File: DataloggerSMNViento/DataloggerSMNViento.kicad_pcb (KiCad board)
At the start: 2 copper layers, 85.7 x 137.2 mm, 26 parts, among them P1 CONN_02X20, P10 CONN_01X20, P11 CONN_01X20, P12 CONN_01X06, P13 CONN_01X06, P14 CONN_02X12, P15 CONN_02X12, P16 CONN_02X12, P17 CONN_02X12, P18 CONN_01X12, P19 CONN_01X12, P2 CONN_01X20, P20 CONN_01X12, P21 CONN_01X12, P3 CONN_02X20, P4 CONN_02X20, P5 CONN_01X19, P6 CONN_02X20, P7 CONN_01X20, P8 CONN_02X20, P9 CONN_02X20

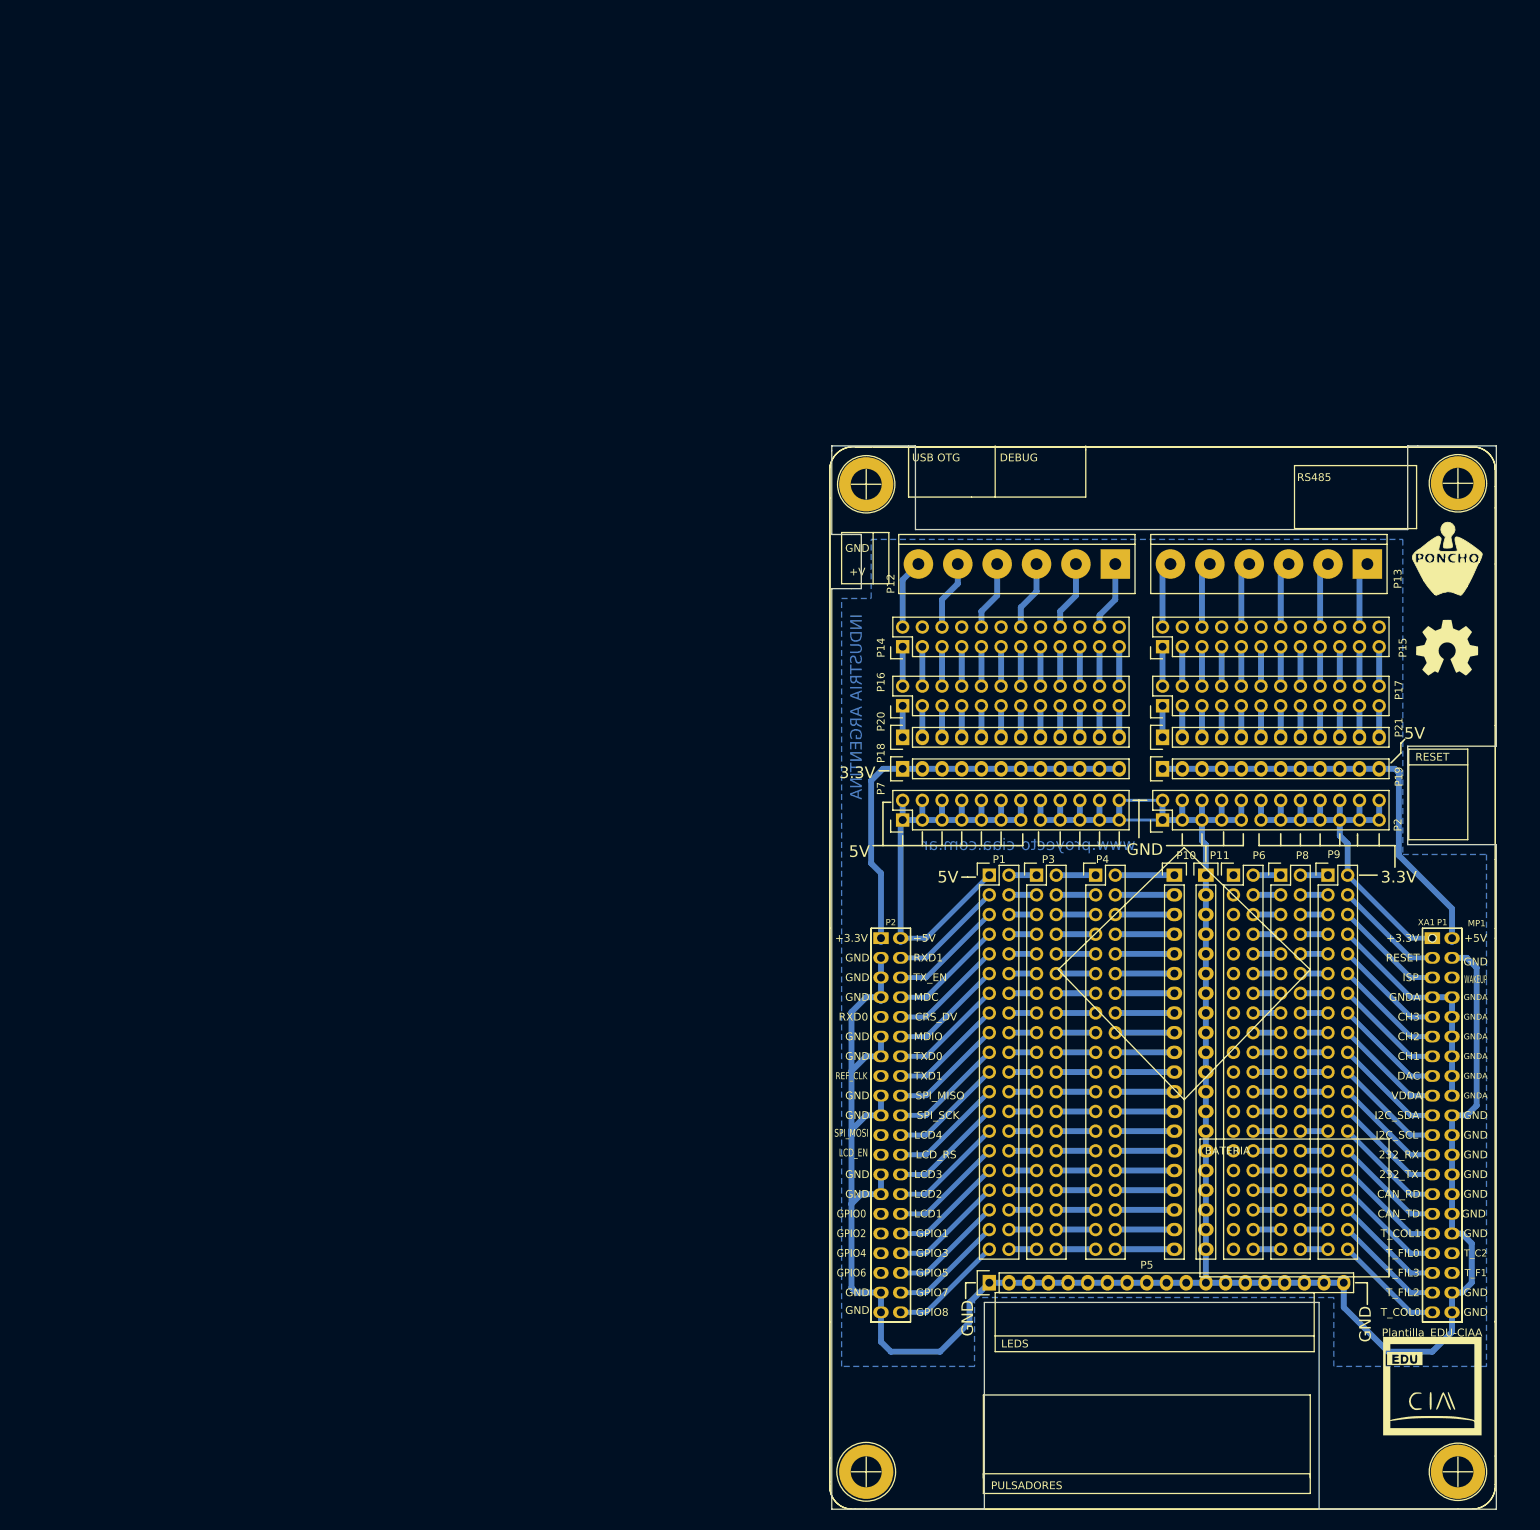
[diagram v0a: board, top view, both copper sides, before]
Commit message: Agrego modificaciones al poncho de la EDU CIAA, también agrego una simulacion del circuito para tomar la tensión del ADC del tunnel
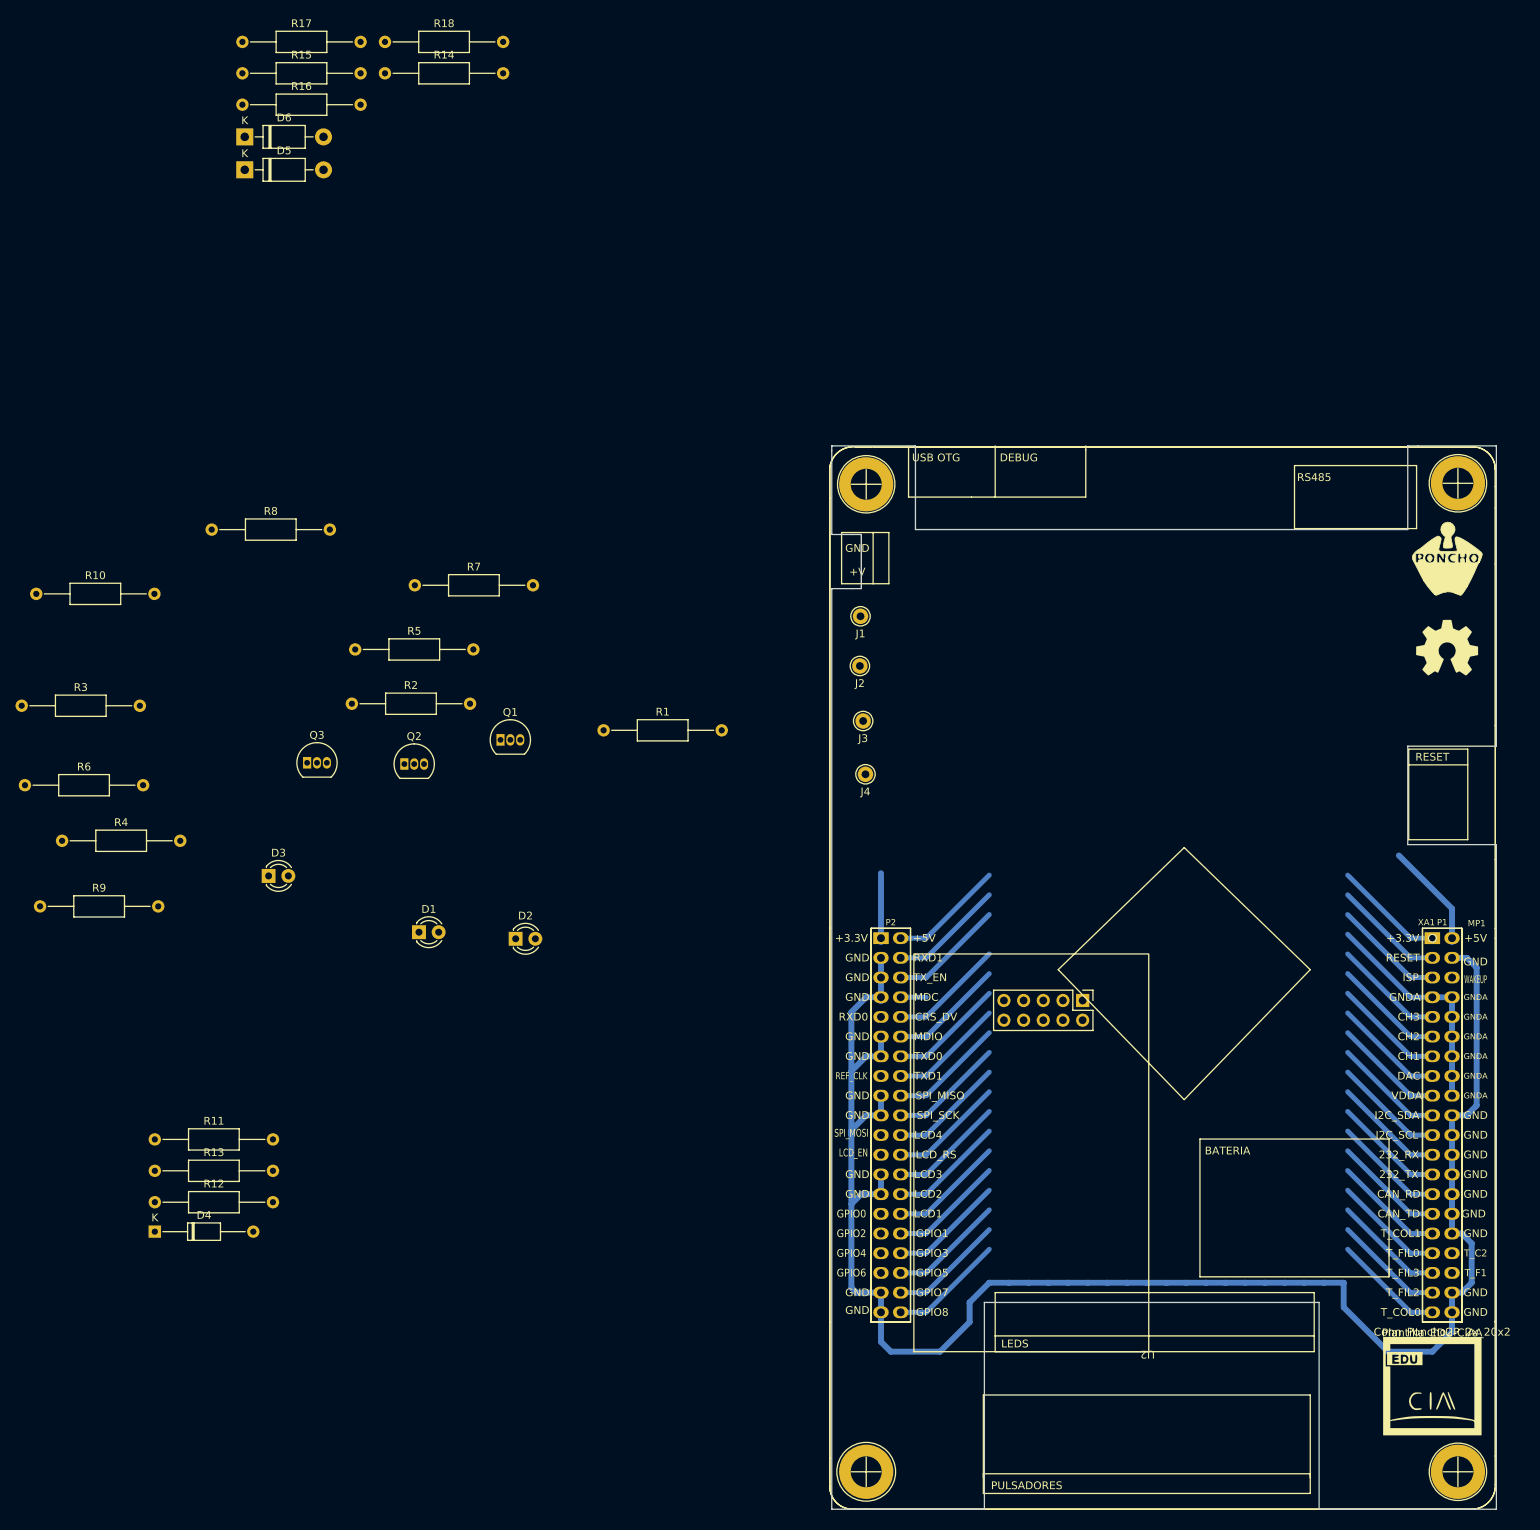
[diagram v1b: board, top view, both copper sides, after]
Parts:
- removed P1, P3, P4, P6, P8, P9: CONN_02X20, Pin_Headers:Pin_Header_Straight_2x20
- removed P10, P11: CONN_01X20, Pin_Headers:Pin_Header_Straight_1x20
- removed P12, P13: CONN_01X06, mod:bornier6
- removed P14, P15, P16, P17: CONN_02X12, Pin_Headers:Pin_Header_Straight_2x12
- removed P18, P19, P20, P21: CONN_01X12, Pin_Headers:Pin_Header_Straight_1x12
- removed P2, P7: CONN_01X20, Pin_Headers:Pin_Header_Straight_2x12
- removed P5: CONN_01X19, Pin_Headers:Pin_Header_Straight_1x19
- added D1: LED, LED_THT:LED_D3.0mm, F.Cu at (20.4, 88.1)
- added D2: LED, LED_THT:LED_D3.0mm, F.Cu at (32.9, 89.0)
- added D3: LED, LED_THT:LED_D3.0mm, F.Cu at (1.02, 80.9)
- added D4: D_Zener, Diode_THT:D_DO-35_SOD27_P12.70mm_Horizontal, F.Cu at (-13.7, 126.8)
- added D5: D_Schottky, Diode_THT:D_DO-41_SOD81_P10.16mm_Horizontal, F.Cu at (-2.06, -10.2)
- added D6: D_Schottky, Diode_THT:D_DO-41_SOD81_P10.16mm_Horizontal, F.Cu at (-2.06, -14.5)
- added J1: Conn_01x01_Male, Connector_Pin:Pin_D1.0mm_L10.0mm, F.Cu at (77.4, 47.4)
- added J2: Conn_01x01_Male, Connector_Pin:Pin_D1.0mm_L10.0mm, F.Cu at (77.3, 53.8)
- added J3: Conn_01x01_Male, Connector_Pin:Pin_D1.0mm_L10.0mm, F.Cu at (77.7, 60.9)
- added J4: Conn_01x01_Male, Connector_Pin:Pin_D1.0mm_L10.0mm, F.Cu at (78.0, 67.8)
- added Q1: 2N7000, Package_TO_SOT_THT:TO-92_Inline, F.Cu at (30.9, 63.3)
- added Q2: 2N7000, Package_TO_SOT_THT:TO-92_Inline, F.Cu at (18.5, 66.4)
- added Q3: 2N7000, Package_TO_SOT_THT:TO-92_Inline, F.Cu at (5.99, 66.3)
- added R1: 1K, Resistor_THT:R_Axial_DIN0207_L6.3mm_D2.5mm_P15.24mm_Horizontal, F.Cu at (44.2, 62.1)
- added R10: 680, Resistor_THT:R_Axial_DIN0207_L6.3mm_D2.5mm_P15.24mm_Horizontal, F.Cu at (-28.9, 44.5)
- added R11: 1k, Resistor_THT:R_Axial_DIN0207_L6.3mm_D2.5mm_P15.24mm_Horizontal, F.Cu at (-13.7, 114.9)
- added R12: 3k9, Resistor_THT:R_Axial_DIN0207_L6.3mm_D2.5mm_P15.24mm_Horizontal, F.Cu at (-13.7, 123.0)
- added R13: 10k, Resistor_THT:R_Axial_DIN0207_L6.3mm_D2.5mm_P15.24mm_Horizontal, F.Cu at (-13.7, 118.9)
- added R14: 10k, Resistor_THT:R_Axial_DIN0207_L6.3mm_D2.5mm_P15.24mm_Horizontal, F.Cu at (16.0, -22.7)
- added R15: 220, Resistor_THT:R_Axial_DIN0207_L6.3mm_D2.5mm_P15.24mm_Horizontal, F.Cu at (-2.36, -22.7)
- added R16: 4k7, Resistor_THT:R_Axial_DIN0207_L6.3mm_D2.5mm_P15.24mm_Horizontal, F.Cu at (-2.36, -18.6)
- added R17: 100k, Resistor_THT:R_Axial_DIN0207_L6.3mm_D2.5mm_P15.24mm_Horizontal, F.Cu at (-2.36, -26.7)
- added R18: 1k, Resistor_THT:R_Axial_DIN0207_L6.3mm_D2.5mm_P15.24mm_Horizontal, F.Cu at (16.0, -26.7)
- added R2: 330K, Resistor_THT:R_Axial_DIN0207_L6.3mm_D2.5mm_P15.24mm_Horizontal, F.Cu at (11.8, 58.7)
- added R3: 10K, Resistor_THT:R_Axial_DIN0207_L6.3mm_D2.5mm_P15.24mm_Horizontal, F.Cu at (-30.8, 58.9)
- added R4: 680, Resistor_THT:R_Axial_DIN0207_L6.3mm_D2.5mm_P15.24mm_Horizontal, F.Cu at (-25.6, 76.3)
- added R5: 330K, Resistor_THT:R_Axial_DIN0207_L6.3mm_D2.5mm_P15.24mm_Horizontal, F.Cu at (12.2, 51.7)
- added R6: 10K, Resistor_THT:R_Axial_DIN0207_L6.3mm_D2.5mm_P15.24mm_Horizontal, F.Cu at (-30.4, 69.2)
- added R7: 680, Resistor_THT:R_Axial_DIN0207_L6.3mm_D2.5mm_P15.24mm_Horizontal, F.Cu at (19.9, 43.4)
- added R8: 330K, Resistor_THT:R_Axial_DIN0207_L6.3mm_D2.5mm_P15.24mm_Horizontal, F.Cu at (-6.32, 36.2)
- added R9: 10K, Resistor_THT:R_Axial_DIN0207_L6.3mm_D2.5mm_P15.24mm_Horizontal, F.Cu at (-28.5, 84.8)
- added U2: w5100_module, Modulos:W5100_module, F.Cu at (114.1, 114.9)
- XA1: value (none) -> Conn_Poncho2P_2x_20x2
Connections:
- XA1 pad 11: /Circuito Principal/ADC2 -> /Conector del Poncho/ADC2
- XA1 pad 13: /Circuito Principal/ADC1 -> /Conector del Poncho/ADC1
- XA1 pad 15: /Circuito Principal/DAC -> unconnected-(XA1-Pad15)
- XA1 pad 17: +3.3VADC -> unconnected-(XA1-Pad17)
- XA1 pad 19: /Circuito Principal/SDA -> unconnected-(XA1-Pad19)
- XA1 pad 21: /Circuito Principal/SCL -> unconnected-(XA1-Pad21)
- XA1 pad 23: /Circuito Principal/RXD -> /Anemometro IBC/232_RX
- XA1 pad 25: /Circuito Principal/TXD -> /Conector del Poncho/TXD
- XA1 pad 27: /Circuito Principal/RD -> unconnected-(XA1-Pad27)
- XA1 pad 29: /Circuito Principal/TD -> unconnected-(XA1-Pad29)
- XA1 pad 3: /Circuito Principal/RESET -> unconnected-(XA1-Pad3)
- XA1 pad 31: /Circuito Principal/COL1 -> /Conector del Poncho/COL1
- XA1 pad 33: /Circuito Principal/F0 -> unconnected-(XA1-Pad33)
- XA1 pad 34: (no net) -> unconnected-(XA1-Pad34)
- XA1 pad 35: /Circuito Principal/F3 -> /Conector del Poncho/F3
- XA1 pad 36: (no net) -> unconnected-(XA1-Pad36)
- XA1 pad 37: /Circuito Principal/F2 -> /Conector del Poncho/F2
- XA1 pad 39: /Circuito Principal/COL0 -> /Conector del Poncho/COL0
- XA1 pad 41: +3.3VP -> +3.3V
- XA1 pad 42: +5VP -> +5V
- XA1 pad 44: /Circuito Principal/RXD1 -> unconnected-(XA1-Pad44)
- XA1 pad 46: /Circuito Principal/TXEN -> unconnected-(XA1-Pad46)
- XA1 pad 48: /Circuito Principal/MDC -> unconnected-(XA1-Pad48)
- XA1 pad 49: (no net) -> unconnected-(XA1-Pad49)
- XA1 pad 5: /Circuito Principal/ISP -> unconnected-(XA1-Pad5)
- XA1 pad 50: /Circuito Principal/CRS -> unconnected-(XA1-Pad50)
- XA1 pad 52: /Circuito Principal/MDIO -> unconnected-(XA1-Pad52)
- XA1 pad 54: /Circuito Principal/TXD0 -> unconnected-(XA1-Pad54)
- XA1 pad 55: (no net) -> unconnected-(XA1-Pad55)
- XA1 pad 56: /Circuito Principal/TXD1 -> unconnected-(XA1-Pad56)
- XA1 pad 58: /Circuito Principal/MISO -> /Conector del Poncho/MISO
- XA1 pad 6: (no net) -> unconnected-(XA1-Pad6)
- XA1 pad 60: /Circuito Principal/spiCCK -> /Conector del Poncho/spiSCK
- XA1 pad 61: (no net) -> /Conector del Poncho/MOSI
- XA1 pad 62: /Circuito Principal/LCD4 -> unconnected-(XA1-Pad62)
- XA1 pad 63: (no net) -> unconnected-(XA1-Pad63)
- XA1 pad 64: /Circuito Principal/RS -> unconnected-(XA1-Pad64)
- XA1 pad 66: /Circuito Principal/LCD3 -> unconnected-(XA1-Pad66)
- XA1 pad 68: /Circuito Principal/LCD2 -> unconnected-(XA1-Pad68)
- XA1 pad 69: (no net) -> /Conector del Poncho/GPIO0
- XA1 pad 70: /Circuito Principal/LCD1 -> unconnected-(XA1-Pad70)
- XA1 pad 71: (no net) -> /Conector del Poncho/GPIO2
- XA1 pad 72: /Circuito Principal/GPIO1 -> unconnected-(XA1-Pad72)
- XA1 pad 73: (no net) -> /Conector del Poncho/GPIO4
- XA1 pad 74: /Circuito Principal/GPIO3 -> unconnected-(XA1-Pad74)
- XA1 pad 75: (no net) -> /Conector del Poncho/GPIO6
- XA1 pad 76: /Circuito Principal/GPIO5 -> unconnected-(XA1-Pad76)
- XA1 pad 78: /Circuito Principal/GPIO7 -> unconnected-(XA1-Pad78)
- XA1 pad 80: /Circuito Principal/GPIO8 -> unconnected-(XA1-Pad80)
- XA1 pad 9: /Circuito Principal/ADC3 -> unconnected-(XA1-Pad9)
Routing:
- net GND: track 336.4 -> 219.6 mm
- net +5VP: track 64.0 -> 0.00 mm
- net +3.3VP: track 54.0 -> 0.00 mm
- net +3.3V: track 54.8 -> 23.2 mm
- net +5V: track 55.4 -> 28.8 mm
- net unconnected-(XA1-Pad76): track 0.00 -> 14.8 mm
- net /Circuito Principal/GPIO5: track 14.8 -> 0.00 mm
- net unconnected-(XA1-Pad78): track 0.00 -> 14.8 mm
- net unconnected-(XA1-Pad72): track 0.00 -> 14.8 mm
- net unconnected-(XA1-Pad70): track 0.00 -> 14.8 mm
- net unconnected-(XA1-Pad68): track 0.00 -> 14.8 mm
- net unconnected-(XA1-Pad66): track 0.00 -> 14.8 mm
- net unconnected-(XA1-Pad64): track 0.00 -> 14.8 mm
- net unconnected-(XA1-Pad62): track 0.00 -> 14.8 mm
- net unconnected-(XA1-Pad56): track 0.00 -> 14.8 mm
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- removed copper zone on B.Cu, net GND
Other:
- board text removed: "3.3V"
- board text removed: "5V"
- board text removed: "GND"
- board text removed: "INDUSTRIA ARGENTINA"
- board text removed: "www.proyecto-ciaa.com.ar"
